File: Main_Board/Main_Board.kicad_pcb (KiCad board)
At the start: 4 copper layers, 63 parts, among them IC1 AZ1085CD-3.3TRG1, J1 Conn_01x08, J2 Conn_01x03_Male, U1 STM32L152ZCTx, U2 LM386, Y1 Crystal

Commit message: ''Updates 12-10"
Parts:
- removed J1: Conn_01x08, Connector_PinHeader_2.54mm:PinHeader_1x08_P2.54mm_Vertical
- removed J2: Conn_01x03_Male, Connector_PinHeader_2.54mm:PinHeader_1x03_P2.54mm_Vertical
- removed LED_Header2: Conn_01x09_Male, Connector_PinHeader_2.54mm:PinHeader_1x09_P2.54mm_Vertical
- removed R1: 1M, SamacSys_Parts:RESC5025X70N
- removed e1: SW_MEC_5G, Button_Switch_SMD:SW_SPST_Omron_B3FS-105xP
- added 5VOut1: Conn_01x02, Connector_PinHeader_2.54mm:PinHeader_1x02_P2.54mm_Vertical, F.Cu at (164.5, 39.6)
- added 7_Seg_Header1: Conn_01x09_Male, Connector_PinHeader_2.54mm:PinHeader_1x09_P2.54mm_Vertical, F.Cu at (99.3, 98.4)
- added C21: 1u, SamacSys_Parts:CAPC1005X55N, F.Cu at (140.3, 37.8)
- added C22: 10u, SamacSys_Parts:CAPC2012X140N, F.Cu at (140.3, 36.3)
- added C23: 22u, SamacSys_Parts:C1608_Commercial, F.Cu at (154.4, 47.8)
- added GPIOHeader1: Conn_01x09, Connector_PinHeader_2.54mm:PinHeader_1x09_P2.54mm_Vertical, F.Cu at (133.0, 98.4)
- added Hal_Out_Header1: Conn_01x08, Connector_PinHeader_2.54mm:PinHeader_1x08_P2.54mm_Vertical, F.Cu at (88.1, 71.4)
- added Hall_Sel_Header1: Conn_01x03_Male, Connector_PinHeader_2.54mm:PinHeader_1x03_P2.54mm_Vertical, F.Cu at (113.0, 26.7)
- added nRST1: PTS647SM50SMTR2LFS, PTS647SM50SMTR2LFS, F.Cu at (140.4, 67.6)
- C11, C24: value 30p -> 4p; footprint Capacitor_SMD:C_1206_3216Metric_Pad1.33x1.80mm_HandSolder -> CAPC1005X55N
- C16: value 250u -> 220u; footprint Capacitor_THT:CP_Radial_D4.0mm_P2.00mm -> CAPPRD200W55D500H1200
- C17, C20: footprint SamacSys_Parts:CAPC2012X95N -> SamacSys_Parts:C1608_Commercial
- C25: value C_Small -> 100n; footprint SamacSys_Parts:CAPC2012X140N -> SamacSys_Parts:CAPC2012X95N
- CA1: footprint SamacSys_Parts:CAPC2012X140N -> SamacSys_Parts:CAPC0402X22N
- LA0: footprint Inductor_SMD:L_01005_0402Metric_Pad0.57x0.30mm_HandSolder -> SamacSys_Parts:LQW2UAS12NG00L
- LED3V3: footprint LED Lib:XCXZCFBB53W-8VF -> LEDM168X65N
- LED5V1: footprint LED Lib:XCXZCFBB53W-8VF -> SamacSys_Parts:HSMA-C380
- R2: value R -> 680; footprint Resistor_THT:R_Axial_DIN0309_L9.0mm_D3.2mm_P12.70mm_Horizontal -> RESC3116X70N
- R3: value R -> 82; footprint Resistor_THT:R_Axial_DIN0309_L9.0mm_D3.2mm_P12.70mm_Horizontal -> RESC6432X65N
- R7: footprint Resistor_THT:R_Axial_DIN0309_L9.0mm_D3.2mm_P12.70mm_Horizontal -> RESC5025X120N
- R8: value R_Small -> 10k; footprint SamacSys_Parts:RESC5025X70N -> SamacSys_Parts:RESC3116X70N
- Y1: value Crystal -> ABM10W-16.0000MHZ-4-B1U-T3; footprint Crystal:Crystal_HC18-U_Vertical -> ABM10W400000MHZ4K1ZT3
- moved SD_CARD1 26.8 mm to (166.1, 75.9), turned to 90 degrees
- moved JTAGHEADER1 11.5 mm to (136.8, 82.2)
- moved R8 11.4 mm to (149.1, 64.9), turned to 0 degrees
- moved C25 9.56 mm to (144.9, 65.8)
- moved R7 7.26 mm to (126.8, 40.6), turned to 0 degrees
- moved C11 7.06 mm to (117.9, 49.9), turned to 90 degrees
- moved Y1 6.38 mm to (117.0, 53.5)
- moved C24 6.01 mm to (115.3, 49.9), turned to 90 degrees
- moved LED3V3 3.89 mm to (159.5, 57.5)
- moved LED5V1 3.67 mm to (163.7, 54.2), turned to 0 degrees
- moved LA0 3.14 mm to (111.1, 50.7), turned to 0 degrees
- moved CA1 2.43 mm to (112.5, 53.9), turned to 0 degrees
- moved R3 1.79 mm to (159.4, 64.3)
- moved C16 1.73 mm to (115.6, 33.5), turned to 90 degrees
- moved R2 0.93 mm to (163.3, 63.9)
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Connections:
- net /OSC_IN renamed OSC_IN
- C16 pad 1: Net-(C16-Pad1) -> Net-(C15-Pad1)
- C16 pad 2: Net-(C15-Pad1) -> Net-(C16-Pad2)
- C24 pad 1: /OSC_OUT -> OSC_OUT
- Speaker+1 pad 1: Net-(C16-Pad1) -> Net-(C16-Pad2)
- U1 pad 138: Boot -> GND
- U1 pad 24: /OSC_OUT -> OSC_OUT
- U1 pad 31: Net-(U1-Pad31) -> GND
- U1 pad 32: Net-(U1-Pad32) -> +3.3VA
- U1 pad 88: Net-(U1-Pad88) -> S1[1]
- U1 pad 89: Net-(U1-Pad89) -> S1[2]
- U1 pad 90: Net-(U1-Pad90) -> S1[3]
- U1 pad 91: Net-(U1-Pad91) -> S2[1]
- U1 pad 92: Net-(U1-Pad92) -> S2[2]
- U1 pad 93: Net-(U1-Pad93) -> S2[3]
- Y1 pad 2: /OSC_OUT -> GND
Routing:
- net S2[3]: track 0.00 -> 40.4 mm, vias 0 -> 1
- net S2[2]: track 0.00 -> 38.8 mm, vias 0 -> 1
- net S2[1]: track 0.00 -> 37.2 mm, vias 0 -> 1
- net S1[3]: track 0.00 -> 35.8 mm, vias 0 -> 1
- net S1[2]: track 0.00 -> 34.7 mm, vias 0 -> 1
- net S1[1]: track 0.00 -> 33.4 mm, vias 0 -> 1
- net GND: track 171.0 -> 152.6 mm, vias 38 -> 44
- net /OSC_OUT: track 13.6 -> 0.00 mm
- net Net-(C15-Pad2): track 14.6 -> 5.08 mm
- net nRST: track 64.6 -> 55.1 mm
- net OSC_OUT: track 0.00 -> 7.28 mm
- net Net-(C16-Pad2): track 0.00 -> 7.05 mm
- net Net-(C16-Pad1): track 7.00 -> 0.00 mm
- net Net-(U1-Pad9): track 0.00 -> 5.85 mm, vias 0 -> 1
- net Net-(U1-Pad124): track 0.00 -> 5.73 mm, vias 0 -> 1
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- added copper zone on F.Cu, net +3V3
- added copper zone on F.Cu, net GND
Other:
- board text added: "TL"
- board text added: "TR"

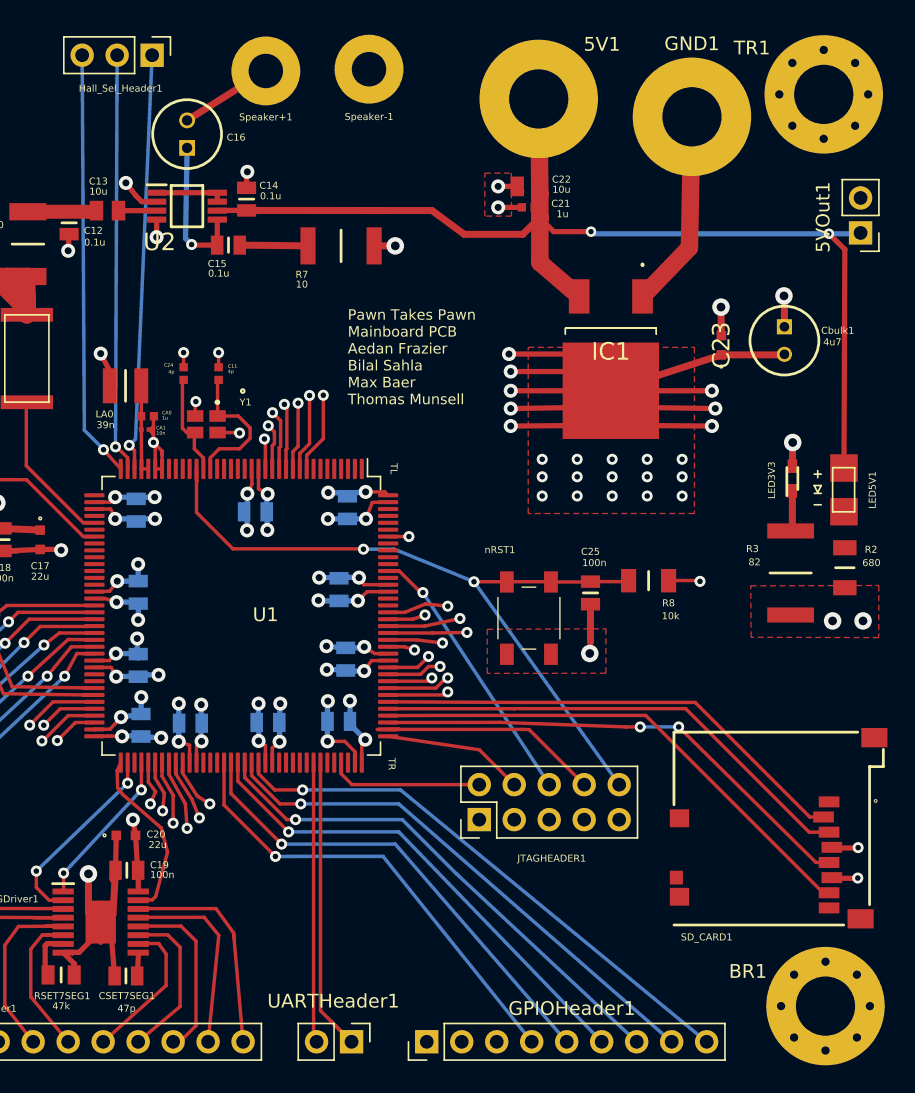
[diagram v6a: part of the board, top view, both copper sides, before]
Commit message: added DC jack, miscellaneous
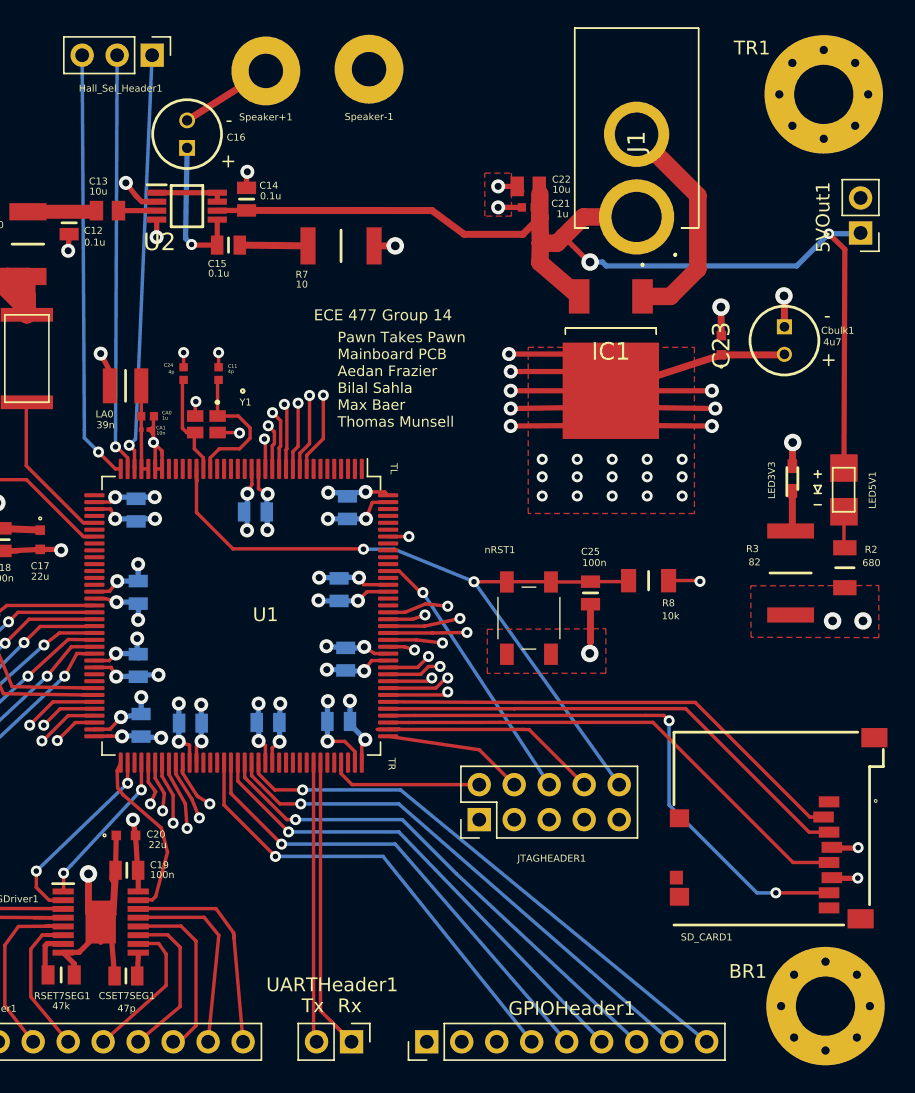
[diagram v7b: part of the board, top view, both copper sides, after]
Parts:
- removed 5V1, GND1: MountingHole_Pad, MountingHole:MountingHole_4.3mm_M4_Pad
- added J1: PJ-037A, Main_Board:PJ037A, F.Cu at (148.2, 38.5)
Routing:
- net SPI3_MISO: track 37.3 -> 41.4 mm, vias 0 -> 2
- net Net-(LED5V1-Pad1): track 0.00 -> 2.64 mm
- net GND: track 152.6 -> 154.7 mm
- net +5V: track 81.4 -> 82.0 mm
- net SPI3_SCK: track 36.1 -> 36.6 mm, vias 2 -> 0
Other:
- board text added: "+"
- board text added: "-"
- board text added: "ECE 477 Group 14"
- board text added: "Rx"
- board text added: "Tx"

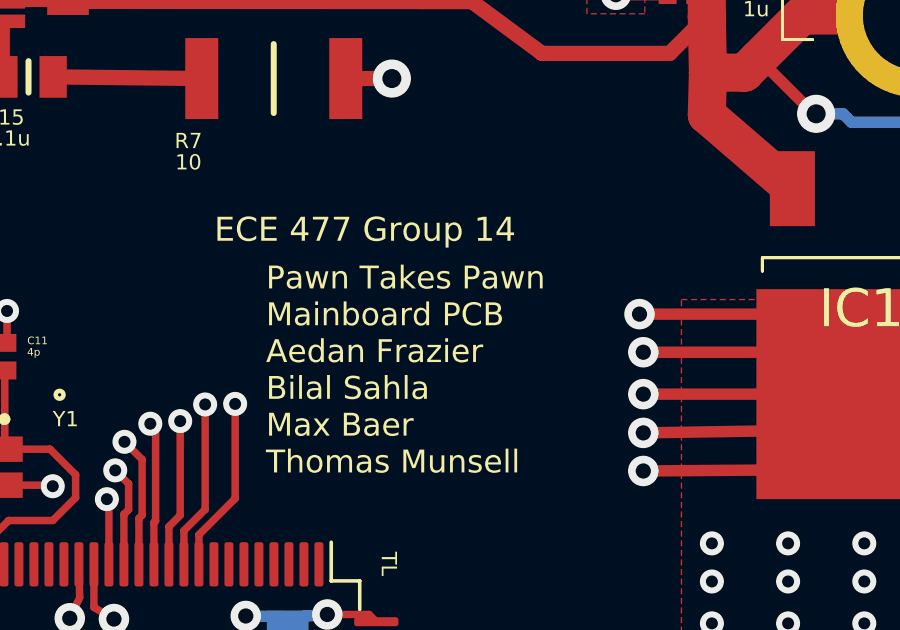
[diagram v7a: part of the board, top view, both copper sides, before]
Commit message: cleaned up directories, silkscreen
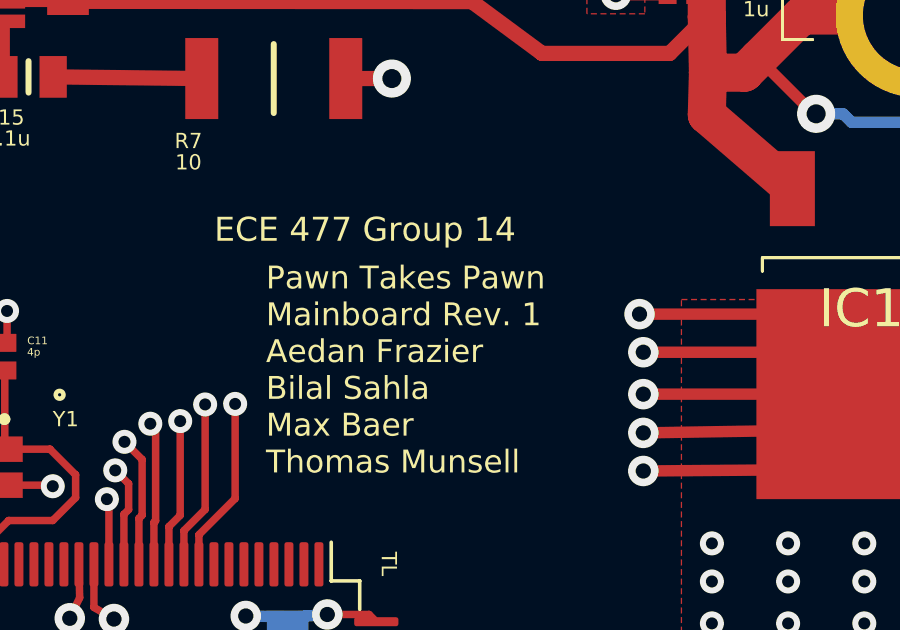
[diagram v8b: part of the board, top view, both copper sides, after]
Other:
- board text added: "Pawn Takes Pawn Mainboard Rev. 1 Aedan Frazier Bilal Sahla Max Baer Thomas Munsell"
- board text removed: "Pawn Takes Pawn Mainboard PCB Aedan Frazier Bilal Sahla Max Baer Thomas Munsell"
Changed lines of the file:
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@@
   )
   (gr_circle (center 119.61368 51.12258) (end 119.743195 51.12258) (layer F.SilkS) (width 0.15))
-  (gr_text "Pawn Takes Pawn\nMainboard PCB\nAedan Frazier\nBilal Sahla\nMax Baer\nThomas Munsell\n" (at 126.492 50.292) (layer F.SilkS)
+  (gr_text "Pawn Takes Pawn\nMainboard Rev. 1\nAedan Frazier\nBilal Sahla\nMax Baer\nThomas Munsell\n" (at 126.492 50.292) (layer F.SilkS)
     (effects (font (size 0.762 0.762) (thickness 0.1905)) (justify left))
   )
